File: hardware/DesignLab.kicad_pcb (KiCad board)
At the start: 2 copper layers, 169.9 x 79.5 mm, 77 parts, among them J1 Micro_SD_Card_Det, J2 Conn_01x04_Female, J3 Conn_01x08, J4 Conn_01x08, P1 USB_C_Plug_USB2.0, Q1 DMG3415U-7, SW1 SW_DPDT_x2, SW11 SW_DPDT_x2, SW12 RESET, SW13 ON, SW14 VOL, SW15 BOOT, SW3 REC, U1 SPH0641LM4H, U10 MCP4018-xxxxLT, U2 RP2040, U3 QRE1113, U4 QRE1113, U5 QRE1113, U6 W25Q80DVSSIG, U7 PAM8302AASCR, U8 AP2112K-3.3, U9 QRE1113, Y1 12Mhz

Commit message: New PCB routing started
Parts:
- BZ1, C1, C10, C11, C12, C13, C14, C15, C16, C2, C20, C21, C22, C23, C24, C25, C26, C27, C29, C3, C4, C5, C6, C7, C8, C9, D1, D2, F1, J1, P1, Q1, R1, R13, R14, R15, R16, R17, R18, R19, R2, R20, R23, R3, R5, R8, R9, U1, U10, U2, U6, U7, U8, Y1: moved to B.Cu
- moved BZ1 247.9 mm to (114.9, 34.8), turned to -90 degrees
- moved C23 241.1 mm to (114.0, 37.6), turned to 180 degrees
- moved C2 239.8 mm to (99.5, 38.0), turned to 180 degrees
- moved U1 237.8 mm to (98.7, 35.2), turned to 90 degrees
- moved R16 236.6 mm to (111.7, 41.4), turned to 90 degrees
- moved C24 235.2 mm to (118.2, 37.6), turned to 0 degrees
- moved U7 229.8 mm to (116.7, 41.2), turned to 0 degrees
- moved R14 224.9 mm to (115.2, 43.8)
- moved C25 223.2 mm to (121.5, 41.1), turned to -90 degrees
- moved C21 221.3 mm to (115.2, 45.3), turned to 180 degrees
- moved R15 221.2 mm to (118.7, 43.8), turned to 180 degrees
- moved R13 217.6 mm to (114.3, 51.5)
- moved C22 216.6 mm to (118.7, 45.3), turned to 180 degrees
- moved C20 215.2 mm to (115.8, 51.5)
- moved U10 213.8 mm to (117.0, 47.8), turned to 180 degrees
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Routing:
- net +3V3: track 519.5 -> 265.5 mm, vias 13 -> 3
- net VCC: track 208.6 -> 47.9 mm, vias 3 -> 0
- net /CLK: track 139.8 -> 8.05 mm, vias 2 -> 1
- net /DOUT: track 135.5 -> 6.97 mm, vias 2 -> 1
- net /D0: track 126.8 -> 5.58 mm, vias 3 -> 1
- net /D3: track 121.1 -> 6.15 mm, vias 2 -> 1
- net /D7: track 120.7 -> 6.35 mm, vias 1 -> 0
- net /D1: track 117.3 -> 3.07 mm
- net /D5: track 123.6 -> 10.3 mm, vias 2 -> 0
- net /D2: track 110.2 -> 4.55 mm, vias 2 -> 1
- net /D4: track 106.5 -> 4.68 mm, vias 2 -> 1
- net /D6: track 101.5 -> 3.79 mm
- net /S4: track 92.3 -> 19.3 mm
- net /S1: track 84.4 -> 14.9 mm, vias 2 -> 1
- net /A2: track 64.6 -> 1.73 mm, vias 2 -> 1
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- removed copper zone on B.Cu, net GND
- removed copper zone on F.Cu, net GND
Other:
- board size 169.9 x 79.5 mm -> 242.7 x 186.5 mm
- board text added: "Assembly holes"
- board text added: "Back (Micro SD, USB, 3 push buttons)"
- board text added: "Battery holder"
- board text added: "Front (4 buttons)"
- board text added: "Push button"
- board text added: "Rotary switch"
- board text added: "Toggle switch"

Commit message: Almost finished the PCB  and started with the PCB of buttons
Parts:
- removed J3, J4: Conn_01x08, Connector_PinHeader_2.54mm:PinHeader_1x08_P2.54mm_Vertical
- moved U1 90.1 mm to (188.4, 43.3), turned to 0 degrees
- moved C2 86.3 mm to (185.6, 44.1), turned to 90 degrees
- moved SW3 12.0 mm to (106.2, 39.0)
- moved SW12 12.0 mm to (106.2, 51.0)
- moved U3 1.98 mm to (170.3, 34.5)
- moved SW11 0.21 mm to (256.2, 53.5)
- moved U5 0.21 mm to (246.3, 36.4)
- moved SW13 0.18 mm to (128.2, 53.0)
- moved U4 0.18 mm to (130.3, 34.6)
- moved SW1 0.15 mm to (214.2, 53.0)
- moved U9 0.13 mm to (206.3, 36.4)
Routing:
- net /S1: track 14.9 -> 122.6 mm, vias 1 -> 4
- net +3V3: track 265.5 -> 372.9 mm, vias 3 -> 5
- net /RST: track 18.1 -> 96.2 mm, vias 1 -> 2
- net /S2: track 22.8 -> 84.1 mm, vias 0 -> 2
- net /CLK: track 8.05 -> 65.6 mm, vias 1 -> 2
- net /DOUT: track 6.97 -> 59.4 mm, vias 1 -> 2
- net /SDA: track 8.93 -> 61.1 mm, vias 0 -> 6
- net /S4: track 19.3 -> 71.3 mm, vias 0 -> 2
- net /S3: track 21.3 -> 69.2 mm, vias 0 -> 2
- net /REC: track 15.4 -> 61.9 mm, vias 0 -> 2
- net /SCL: track 8.67 -> 54.4 mm, vias 0 -> 6
- net VCC: track 47.9 -> 92.9 mm, vias 0 -> 2
- net /VOL: track 15.6 -> 54.8 mm, vias 0 -> 1
- net /A2: track 1.73 -> 40.5 mm, vias 1 -> 4
- net GND: track 11.4 -> 26.3 mm, vias 9 -> 20
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- added copper zone on B.Cu, net GND
- added copper zone on F.Cu, net GND
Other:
- board size 242.7 x 186.5 mm -> 194 x 36 mm
- board text removed: "Assembly holes"
- board text removed: "Back (Micro SD, USB, 3 push buttons)"
- board text removed: "Battery holder"
- board text removed: "Front (4 buttons)"
- board text removed: "Push button"
- board text removed: "Rotary switch"
- board text removed: "Toggle switch"

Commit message: Update button and Kicad7
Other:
- board text added: "LANG 1"
- board text added: "LANG 2"
- board text removed: "LANG 1/LANG 2"

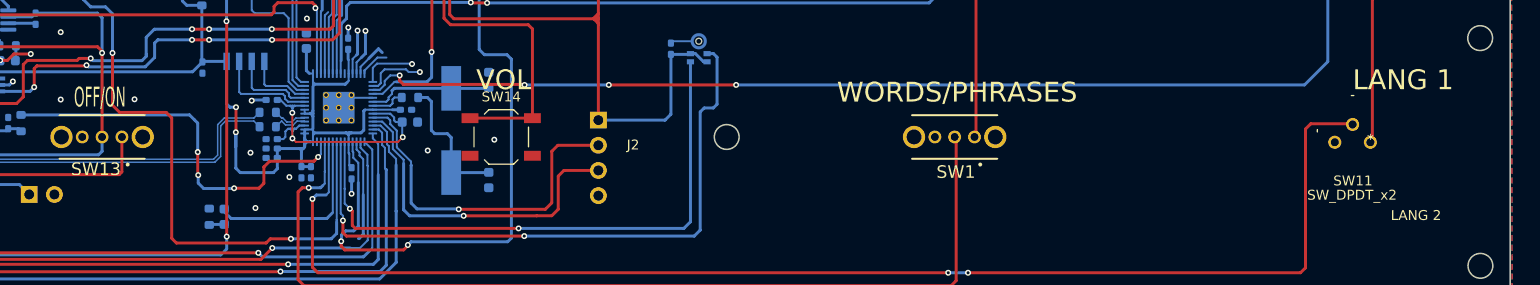
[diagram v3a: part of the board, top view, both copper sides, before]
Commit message: update font
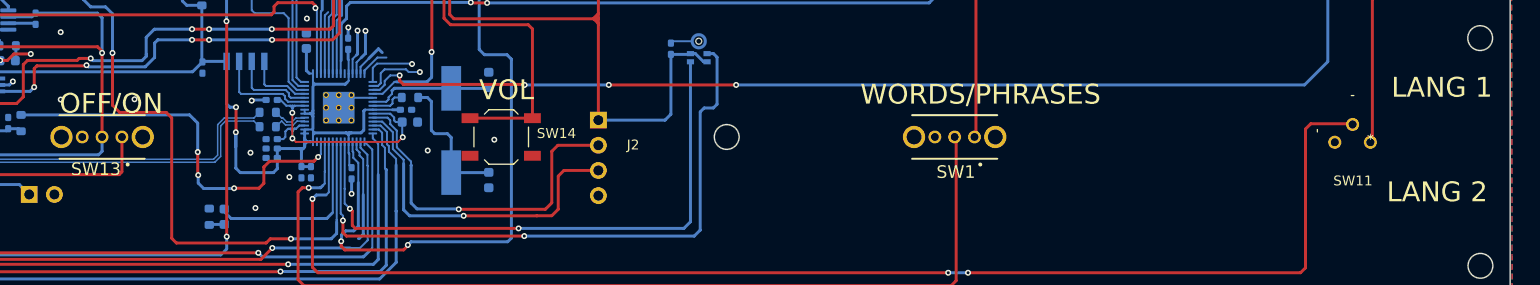
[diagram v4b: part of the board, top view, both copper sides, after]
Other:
- board text added: "BATTERY"
- board text removed: "Battery"

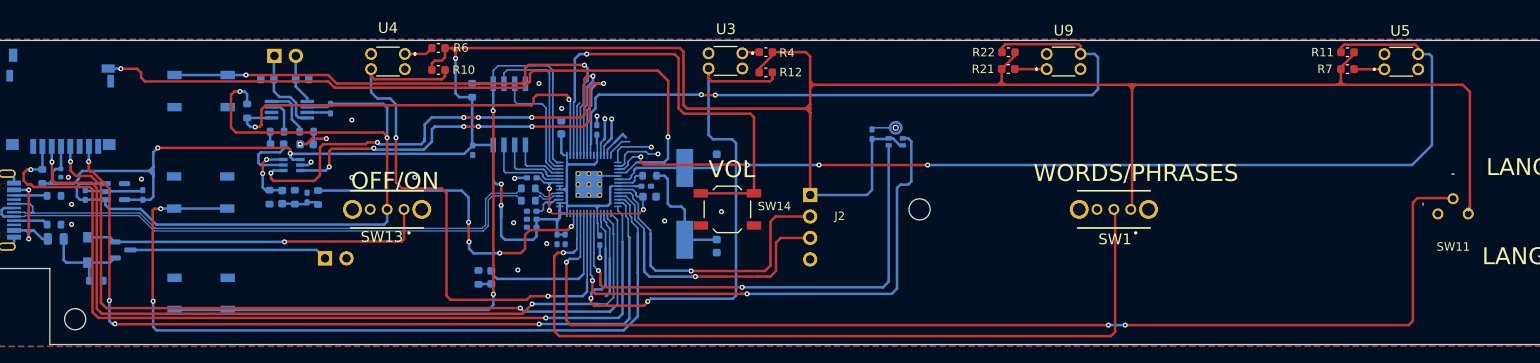
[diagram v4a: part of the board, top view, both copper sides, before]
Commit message: PCB routing finished
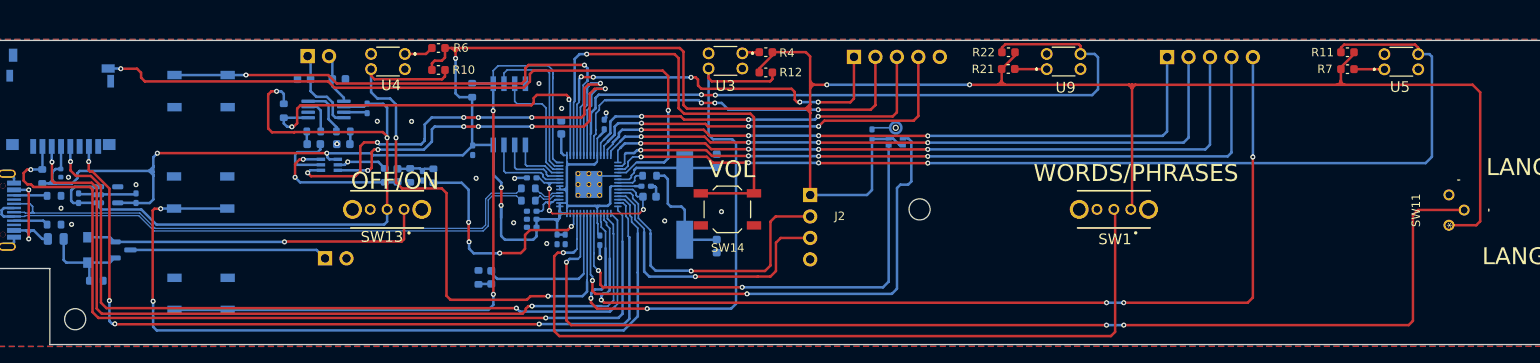
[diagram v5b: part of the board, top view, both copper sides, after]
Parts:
- added J3: Conn_01x05, Connector_PinHeader_2.54mm:PinHeader_1x05_P2.54mm_Vertical, B.Cu at (220.6, 35.0)
- added J5: Conn_01x05, Connector_PinHeader_2.54mm:PinHeader_1x05_P2.54mm_Vertical, B.Cu at (183.5, 35.0)
- moved C16 13.9 mm to (132.4, 49.0), turned to -90 degrees
- moved R13 13.9 mm to (128.0, 49.0), turned to 90 degrees
- moved C20 13.9 mm to (129.4, 49.0), turned to -90 degrees
- moved R8 13.9 mm to (133.7, 49.0), turned to -90 degrees
- moved R9 13.9 mm to (130.9, 49.0), turned to -90 degrees
- moved U10 4.44 mm to (121.4, 47.7)
- moved C23 4.34 mm to (118.4, 37.6)
- moved C24 4.34 mm to (122.5, 37.6)
- moved C21 4.34 mm to (119.5, 45.3)
- moved C22 4.34 mm to (123.0, 45.3)
- moved C25 4.34 mm to (125.9, 41.0)
- moved R14 4.34 mm to (119.5, 43.8)
- moved R15 4.34 mm to (123.0, 43.8)
- moved R16 4.34 mm to (116.0, 41.3)
- moved U7 4.34 mm to (121.0, 41.2)
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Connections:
- U2 pad 11: /D2 -> /D0
- U2 pad 12: /D4 -> /D7
- U2 pad 13: /D6 -> /D4
- U2 pad 15: /D0 -> /D8
- U2 pad 16: /D3 -> /D5
- U2 pad 31: /D5 -> /D2
- U2 pad 4: /D7 -> /D6
- U2 pad 9: unconnected-(U2-Pad9) -> /D3
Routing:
- net /D2: track 4.55 -> 117.1 mm, vias 1 -> 4
- net /D8: track 0.00 -> 82.8 mm, vias 0 -> 4
- net /D1: track 3.07 -> 79.7 mm, vias 0 -> 4
- net /D5: track 10.3 -> 85.8 mm, vias 0 -> 4
- net /D4: track 4.68 -> 77.6 mm, vias 1 -> 4
- net /D6: track 3.79 -> 49.1 mm, vias 0 -> 5
- net /D7: track 6.35 -> 47.7 mm, vias 0 -> 3
- net /D0: track 5.58 -> 45.7 mm, vias 1 -> 3
- net /D3: track 6.15 -> 45.6 mm, vias 1 -> 3
- net /A2: track 40.5 -> 27.8 mm
- net /A: track 7.94 -> 17.2 mm
- net VCC: track 92.9 -> 84.6 mm
- net +3V3: track 372.9 -> 379.8 mm, vias 5 -> 7
- net /SCL: track 54.4 -> 48.9 mm
- net /SDA: track 61.1 -> 55.9 mm
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
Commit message: add labels buttons
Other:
- board text added: "3V3"
- board text added: "CLK"
- board text added: "D0"
- board text added: "D1"
- board text added: "D2"
- board text added: "D3"
- board text added: "D4"
- board text added: "D5"
- board text added: "D6"
- board text added: "D7"
- board text added: "D8"
- board text added: "DIO"
- board text added: "GND"

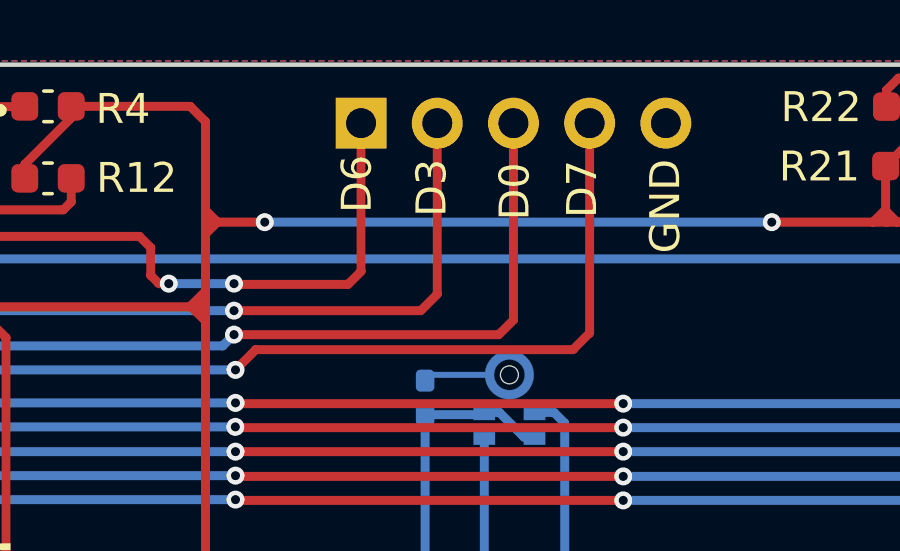
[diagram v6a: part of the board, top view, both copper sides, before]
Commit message: Finished button PCBs
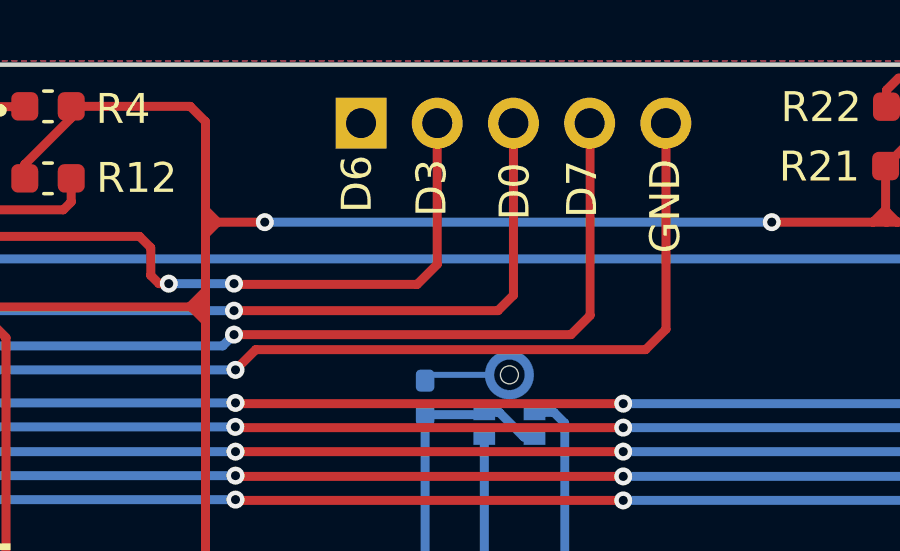
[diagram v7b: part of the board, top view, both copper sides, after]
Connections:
- J5 pad 1: /D6 -> GND
- J5 pad 2: /D3 -> /D6
- J5 pad 3: /D0 -> /D3
- J5 pad 4: /D7 -> /D0
- J5 pad 5: GND -> /D7
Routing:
- net /D3: track 45.6 -> 48.2 mm
- net /D7: track 47.7 -> 50.2 mm
- net /D0: track 45.7 -> 48.2 mm
- net /D6: track 49.1 -> 51.5 mm
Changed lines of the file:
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@@
       (stroke (width 0.1) (type solid)) (layer "B.Fab"))
     (pad "1" thru_hole rect (at 0 0 270) (size 1.7 1.7) (drill 1) (layers "*.Cu" "*.Mask")
-      (net 64 "/D6") (pinfunction "Pin_1") (pintype "passive"))
+      (net 2 "GND") (pinfunction "Pin_1") (pintype "passive"))
     (pad "2" thru_hole oval (at 0 -2.54 270) (size 1.7 1.7) (drill 1) (layers "*.Cu" "*.Mask")
-      (net 60 "/D3") (pinfunction "Pin_2") (pintype "passive"))
+      (net 64 "/D6") (pinfunction "Pin_2") (pintype "passive"))
     (pad "3" thru_hole oval (at 0 -5.08 270) (size 1.7 1.7) (drill 1) (layers "*.Cu" "*.Mask")
-      (net 63 "/D0") (pinfunction "Pin_3") (pintype "passive"))
+      (net 60 "/D3") (pinfunction "Pin_3") (pintype "passive"))
     (pad "4" thru_hole oval (at 0 -7.62 270) (size 1.7 1.7) (drill 1) (layers "*.Cu" "*.Mask")
-      (net 58 "/D7") (pinfunction "Pin_4") (pintype "passive"))
+      (net 63 "/D0") (pinfunction "Pin_4") (pintype "passive"))
     (pad "5" thru_hole oval (at 0 -10.16 270) (size 1.7 1.7) (drill 1) (layers "*.Cu" "*.Mask")
-      (net 2 "GND") (pinfunction "Pin_5") (pintype "passive"))
+      (net 58 "/D7") (pinfunction "Pin_5") (pintype "passive"))
     (model "${KICAD6_3DMODEL_DIR}/Connector_PinHeader_2.54mm.3dshapes/PinHeader_1x05_P2.54mm_Vertical.wrl"
       (offset (xyz 0 0 0))
@@
   (segment (start 166.199503 43.174503) (end 165.9 42.875) (width 0.3) (layer "F.Cu") (net 58))
   (segment (start 165.9 42.875) (end 158.421351 42.875) (width 0.3) (layer "F.Cu") (net 58))
-  (segment (start 190.55 42.5) (end 191.105 41.945) (width 0.3) (layer "F.Cu") (net 58))
-  (segment (start 191.105 41.945) (end 191.105 34.95) (width 0.3) (layer "F.Cu") (net 58))
-  (segment (start 179.975 42.5) (end 190.55 42.5) (width 0.3) (layer "F.Cu") (net 58))
+  (segment (start 193.65 34.955) (end 193.645 34.95) (width 0.3) (layer "F.Cu") (net 58))
   (segment (start 171 43.174503) (end 166.199503 43.174503) (width 0.3) (layer "F.Cu") (net 58))
-  (segment (start 179.3 43.175) (end 179.975 42.5) (width 0.3) (layer "F.Cu") (net 58))
+  (segment (start 192.97 42.5) (end 193.65 41.82) (width 0.3) (layer "F.Cu") (net 58))
   (segment (start 158.421351 42.875) (end 158.339161 42.79281) (width 0.3) (layer "F.Cu") (net 58))
+  (segment (start 179.3 43.175) (end 179.975 42.5) (width 0.3) (layer "F.Cu") (net 58))
+  (segment (start 193.65 41.82) (end 193.65 34.955) (width 0.3) (layer "F.Cu") (net 58))
+  (segment (start 179.975 42.5) (end 192.97 42.5) (width 0.3) (layer "F.Cu") (net 58))
   (via (at 179.3 43.175) (size 0.6) (drill 0.3) (layers "F.Cu" "B.Cu") (net 58))
   (via (at 171 43.174503) (size 0.6) (drill 0.3) (layers "F.Cu" "B.Cu") (net 58))
@@
   (segment (start 155.49 54.2725) (end 154.702 53.4845) (width 0.2) (layer "B.Cu") (net 59))
   (segment (start 90.725 47.325) (end 90.75 47.35) (width 0.3) (layer "B.Cu") (net 59))
+  (segment (start 188.565 40.685) (end 188.05 41.2) (width 0.3) (layer "F.Cu") (net 60))
   (segment (start 167.025 40.4) (end 165.425 40.4) (width 0.3) (layer "F.Cu") (net 60))
-  (segment (start 186.025 34.95) (end 186.025 40.65) (width 0.3) (layer "F.Cu") (net 60))
-  (segment (start 186.025 40.65) (end 185.475 41.2) (width 0.3) (layer "F.Cu") (net 60))
-  (segment (start 185.475 41.2) (end 179.25 41.2) (width 0.3) (layer "F.Cu") (net 60))
+  (segment (start 188.05 41.2) (end 179.25 41.2) (width 0.3) (layer "F.Cu") (net 60))
+  (segment (start 188.565 34.95) (end 188.565 40.685) (width 0.3) (layer "F.Cu") (net 60))
   (via (at 167.025 40.4) (size 0.6) (drill 0.3) (layers "F.Cu" "B.Cu") (net 60))
   (via (at 165.425 40.4) (size 0.6) (drill 0.3) (layers "F.Cu" "B.Cu") (net 60))
@@
   (segment (start 223.09 44.51) (end 223.09 34.975) (width 0.3) (layer "B.Cu") (net 62))
   (segment (start 192.225 45.099503) (end 192.225497 45.1) (width 0.3) (layer "B.Cu") (net 62))
+  (segment (start 191.12 34.965) (end 191.105 34.95) (width 0.3) (layer "F.Cu") (net 63))
+  (segment (start 190.48 42) (end 191.12 41.36) (width 0.3) (layer "F.Cu") (net 63))
   (segment (start 171 42.375) (end 163.367893 42.375) (width 0.3) (layer "F.Cu") (net 63))
+  (segment (start 179.250497 42) (end 190.48 42) (width 0.3) (layer "F.Cu") (net 63))
   (segment (start 163.367893 42.375) (end 162.98636 41.993467) (width 0.3) (layer "F.Cu") (net 63))
-  (segment (start 188.075 42) (end 188.565 41.51) (width 0.3) (layer "F.Cu") (net 63))
-  (segment (start 179.250497 42) (end 188.075 42) (width 0.3) (layer "F.Cu") (net 63))
-  (segment (start 188.565 41.51) (end 188.565 34.95) (width 0.3) (layer "F.Cu") (net 63))
-  (segment (start 179.25 41.999503) (end 179.250497 42) (width 0.3) (layer "F.Cu") (net 63))
+  (segment (start 191.12 41.36) (end 191.12 34.965) (width 0.3) (layer "F.Cu") (net 63))
   (segment (start 162.98636 41.993467) (end 158.355123 41.993467) (width 0.3) (layer "F.Cu") (net 63))
+  (segment (start 179.25 41.999503) (end 179.250497 42) (width 0.3) (layer "F.Cu") (net 63))
   (via (at 158.355123 41.993467) (size 0.6) (drill 0.3) (layers "F.Cu" "B.Cu") (net 63))
   (via (at 171 42.375) (size 0.6) (drill 0.3) (layers "F.Cu" "B.Cu") (net 63))
@@
   (segment (start 176.75 40.3) (end 176.475 40.025) (width 0.3) (layer "F.Cu") (net 64))
   (segment (start 165.025 37.65) (end 164.75 37.375) (width 0.3) (layer "F.Cu") (net 64))
-  (segment (start 183.05 40.325) (end 179.275 40.325) (width 0.3) (layer "F.Cu") (net 64))
   (segment (start 176.475 40.025) (end 176.475 39.1) (width 0.3) (layer "F.Cu") (net 64))
-  (segment (start 179.275 40.325) (end 179.25 40.3) (width 0.3) (layer "F.Cu") (net 64))
   (segment (start 176.475 39.1) (end 176.1 38.725) (width 0.3) (layer "F.Cu") (net 64))
   (segment (start 151.25 37.35) (end 151.2 37.3) (width 0.3) (layer "F.Cu") (net 64))
@@
   (segment (start 176.1 38.725) (end 165.425 38.725) (width 0.3) (layer "F.Cu") (net 64))
   (segment (start 165.025 38.325) (end 165.025 37.65) (width 0.3) (layer "F.Cu") (net 64))
+  (segment (start 186.025 39.655) (end 185.355 40.325) (width 0.3) (layer "F.Cu") (net 64))
   (segment (start 152.625 37.35) (end 151.25 37.35) (width 0.3) (layer "F.Cu") (net 64))
-  (segment (start 183.485 39.89) (end 183.05 40.325) (width 0.3) (layer "F.Cu") (net 64))
-  (segment (start 183.485 34.95) (end 183.485 39.89) (width 0.3) (layer "F.Cu") (net 64))
   (segment (start 177.075 40.3) (end 176.75 40.3) (width 0.3) (layer "F.Cu") (net 64))
+  (segment (start 185.355 40.325) (end 179.275 40.325) (width 0.3) (layer "F.Cu") (net 64))
+  (segment (start 186.025 34.95) (end 186.025 39.655) (width 0.3) (layer "F.Cu") (net 64))
+  (segment (start 179.275 40.325) (end 179.25 40.3) (width 0.3) (layer "F.Cu") (net 64))
   (via (at 151.2 37.3) (size 0.6) (drill 0.3) (layers "F.Cu" "B.Cu") (net 64))
   (via (at 164.2 37.375) (size 0.6) (drill 0.3) (layers "F.Cu" "B.Cu") (net 64))

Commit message: Update label main
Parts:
- added G***: LOGO, LOGO, B.Cu at (235.2, 62.9)
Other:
- board text added: "DesignLab Builds 2023 Re-engineering Education"
- board text added: "Designed at Supplyframe DesignLab Pasadena, California"
